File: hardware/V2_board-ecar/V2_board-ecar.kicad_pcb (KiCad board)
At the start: 2 copper layers, 160 x 100 mm, 90 parts, among them IC1 ATMEGA8A-P, J1 2x BATT IN, J10 24V, J11 18V, J12 5V, J13 Analog-in-2 0-5V, J14 IGBT, J15 Analog-in-3 - 30to5 (batt), J16 Mosfet Out (Fan), J17 2x Switch \n(to 5V), J18 Relay contacts, J19 2x 5V, J2 ST 2x GND, J3 2x 24V filtered, J4 ST 2x GND, J5 PWM-Signal, J6 LED ~3,2V 20mA, J7 Gas Pedal, J8 Gate, J9 BATT, K1 LEG-5, P1 ISP, Q1 BC547, Q2 IRFZ24N, Q3 BC547, U1 LM7818CT, U2 LM2576T-5, U3 TC429

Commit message: pcb: placed all parts
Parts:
- removed D8: D, Diode_THT:D_T-1_P12.70mm_Horizontal
- removed R2: nopop, Resistor_THT:R_Axial_DIN0922_L20.0mm_D9.0mm_P25.40mm_Horizontal
- added J20: ADC Battery, Connector_PinHeader_1.00mm:PinHeader_1x01_P1.00mm_Vertical, F.Cu at (101.0, 24.1)
- added J21: ADC reserve, Connector_PinHeader_1.00mm:PinHeader_1x01_P1.00mm_Vertical, F.Cu at (86.4, 24.1)
- added J22: ADC Gas-pedal, Connector_PinHeader_1.00mm:PinHeader_1x01_P1.00mm_Vertical, F.Cu at (71.8, 29.8)
- J17: value 2x Switch \n(to 5V) -> 2x Switch (to 5V)
- moved D12 154.3 mm to (42.7, 87.4), turned to 0 degrees
- moved C17 145.8 mm to (45.4, 82.9), turned to 0 degrees
- moved R27 140.1 mm to (67.8, 86.1), turned to 90 degrees
- moved R26 137.8 mm to (63.9, 86.1), turned to 90 degrees
- moved D13 128.4 mm to (78.4, 89.8), turned to 180 degrees
- moved R4 127.5 mm to (53.0, 53.8), turned to -90 degrees
- moved R24 127.5 mm to (52.8, 91.4), turned to 180 degrees
- moved C7 127.3 mm to (71.8, 75.3), turned to 0 degrees
- moved R22 126.9 mm to (52.8, 95.5), turned to 180 degrees
- moved C6 126.1 mm to (77.6, 52.7), turned to 180 degrees
- moved IC1 123.8 mm to (57.1, 64.1), turned to 90 degrees
- moved C18 123.1 mm to (76.0, 86.1), turned to 180 degrees
- moved R25 120.9 mm to (68.3, 93.2)
- moved R23 120.6 mm to (68.3, 96.4)
- moved C8 106.3 mm to (73.1, 80.1)
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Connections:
- J14 pad 1: Net-(J14-Pin_1) -> GND
- J14 pad 2: GND -> Net-(J14-Pin_2)
- J8 pad 1: Net-(J14-Pin_1) -> Net-(J14-Pin_2)
- U3 pad 6: Net-(J14-Pin_1) -> Net-(J14-Pin_2)
- U3 pad 7: Net-(J14-Pin_1) -> Net-(J14-Pin_2)
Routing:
- net Net-(J14-Pin_2): track 0.00 -> 13.9 mm
- net Net-(J14-Pin_1): track 13.9 -> 0.00 mm
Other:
- board text added: "${REFERENCE}"

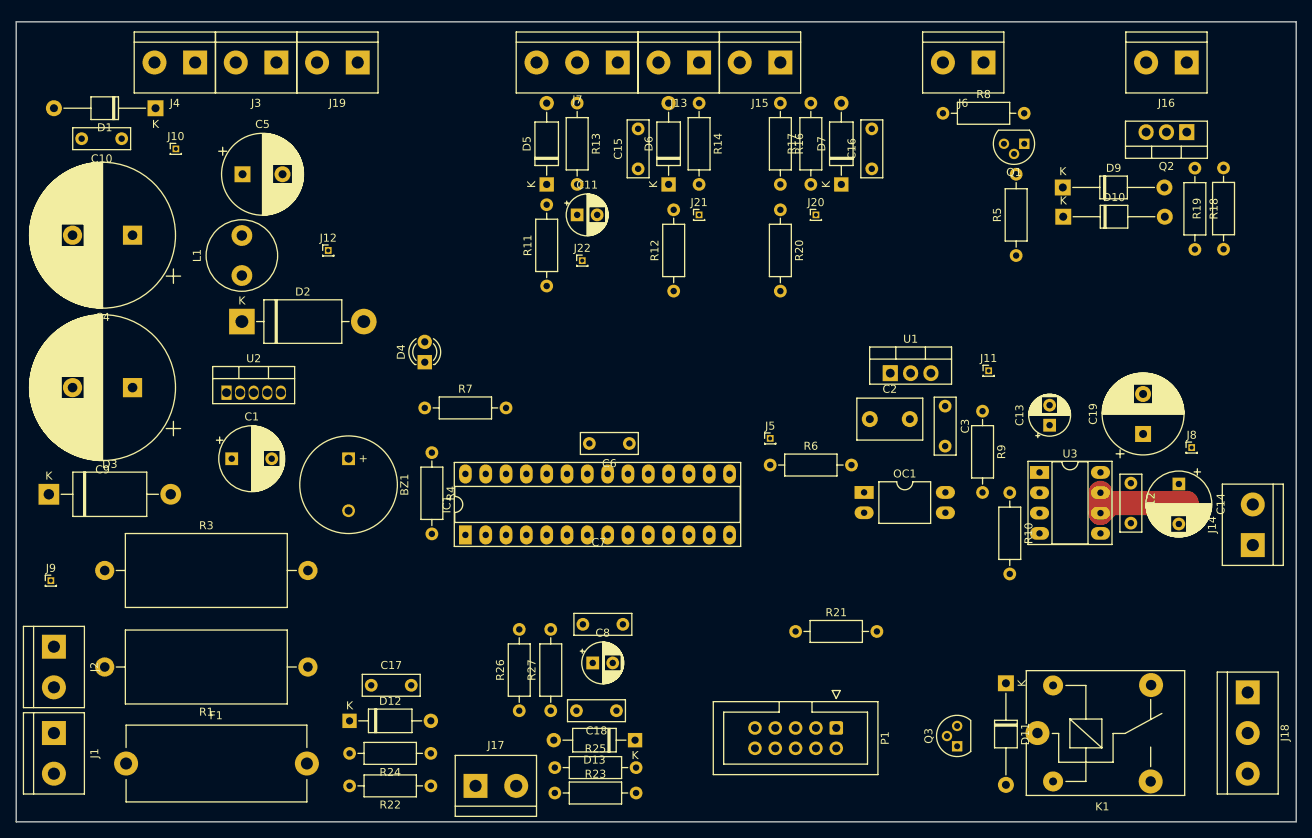
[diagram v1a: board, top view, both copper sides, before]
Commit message: pcb: Add moutingholes, fuses
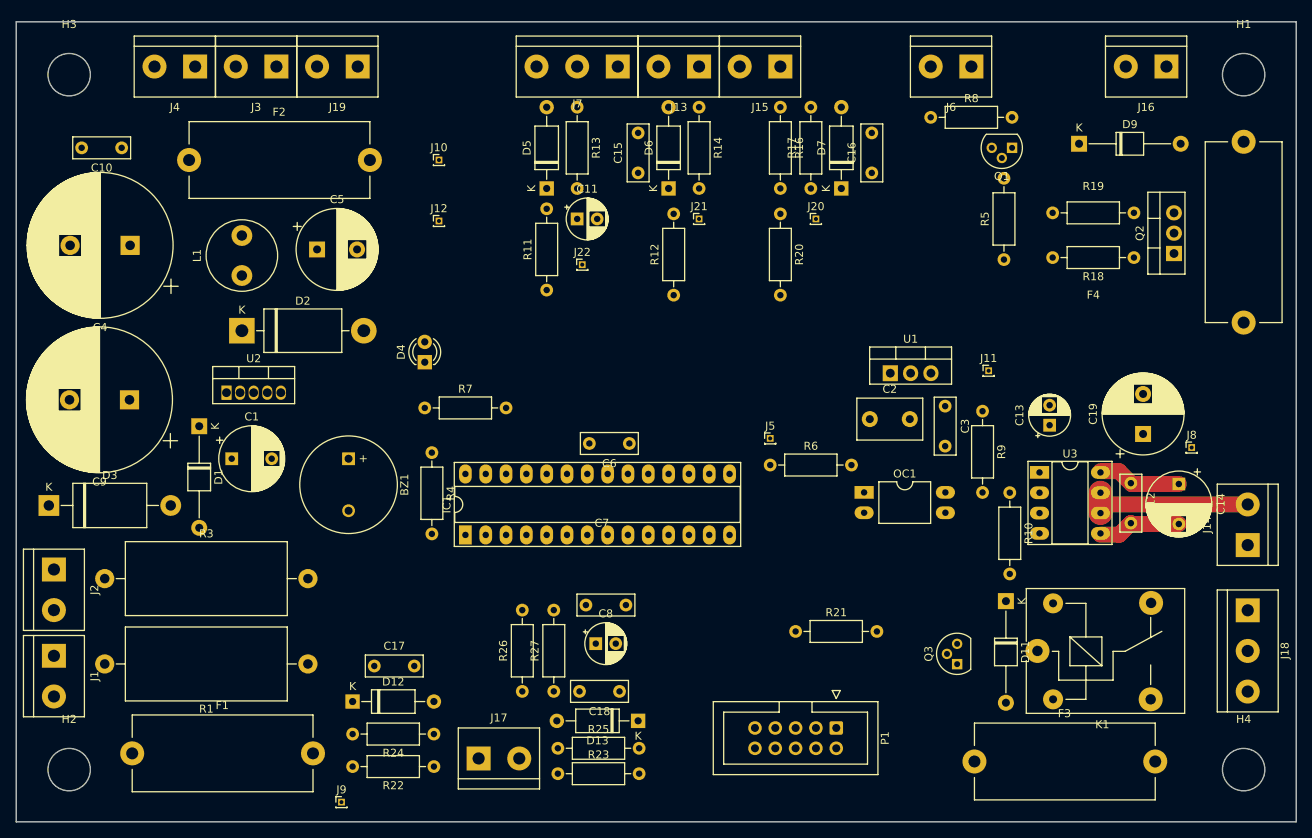
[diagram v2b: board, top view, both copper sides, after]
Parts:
- removed D10: D, Diode_THT:D_T-1_P12.70mm_Horizontal
- added F2: 500mA, Fuse:Fuseholder_Cylinder-5x20mm_Stelvio-Kontek_PTF78_Horizontal_Open, F.Cu at (22.6, 17.3)
- added F3: 500mA, Fuse:Fuseholder_Cylinder-5x20mm_Stelvio-Kontek_PTF78_Horizontal_Open, F.Cu at (120.8, 92.5)
- added F4: 500mA, Fuse:Fuseholder_Cylinder-5x20mm_Stelvio-Kontek_PTF78_Horizontal_Open, F.Cu at (154.4, 37.6)
- added H1: MountingHole, MountingHole:MountingHole_5.3mm_M5, F.Cu at (154.4, 6.60)
- added H2: MountingHole, MountingHole:MountingHole_5.3mm_M5, F.Cu at (7.62, 93.5)
- added H3: MountingHole, MountingHole:MountingHole_5.3mm_M5, F.Cu at (7.62, 6.60)
- added H4: MountingHole, MountingHole:MountingHole_5.3mm_M5, F.Cu at (154.4, 93.5)
- J16: value Mosfet Out (Fan) -> Mosfet Out (Diode, Mosfet)
- moved J9 45.7 mm to (41.7, 97.5)
- moved D1 40.1 mm to (23.9, 50.5), turned to -90 degrees
- moved J10 32.9 mm to (53.8, 17.3)
- moved R19 21.8 mm to (130.6, 23.9), turned to 0 degrees
- moved Q2 15.3 mm to (145.7, 29.0), turned to 90 degrees
- moved J12 14.3 mm to (53.8, 24.9)
- moved R18 13.5 mm to (140.7, 29.5), turned to 180 degrees
- moved C5 13.2 mm to (38.6, 28.4)
- moved D11 10.3 mm to (124.7, 72.4)
- moved K1 10.3 mm to (128.7, 78.6)
- moved J18 10.3 mm to (154.9, 73.6)
- moved Q3 10.3 mm to (118.6, 80.3)
- moved J1 9.65 mm to (5.71, 79.2)
- moved J2 9.65 mm to (5.71, 68.5)
- moved D9 5.83 mm to (133.9, 15.2)
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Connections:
- C10 pad 1: +24V filtered -> Net-(D1-K)
- C4 pad 1: +24V filtered -> Net-(D1-K)
- C9 pad 1: +24V filtered -> Net-(D1-K)
- D1 pad 1: +24V filtered -> Net-(D1-K)
- D3 pad 2: +24V filtered -> Net-(D1-K)
- D9 pad 1: +24V filtered -> Net-(D9-K)
- D9 pad 2: Net-(D10-A) -> Net-(D9-A)
- J16 pad 1: Net-(D10-A) -> Net-(D9-A)
- J16 pad 2: +24V filtered -> Net-(D9-K)
- K1 pad 1: Net-(J18-Pin_2) -> Net-(F3-Pad1)
- Q2 pad 2: Net-(D10-A) -> Net-(Q2-D)
- R3 pad 2: +24V filtered -> Net-(D1-K)
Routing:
- net +18V: track 0.00 -> 10.5 mm
- net GND: track 0.00 -> 10.4 mm
- net Net-(J14-Pin_2): track 13.9 -> 21.4 mm

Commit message: pcb: layout complete (for review)
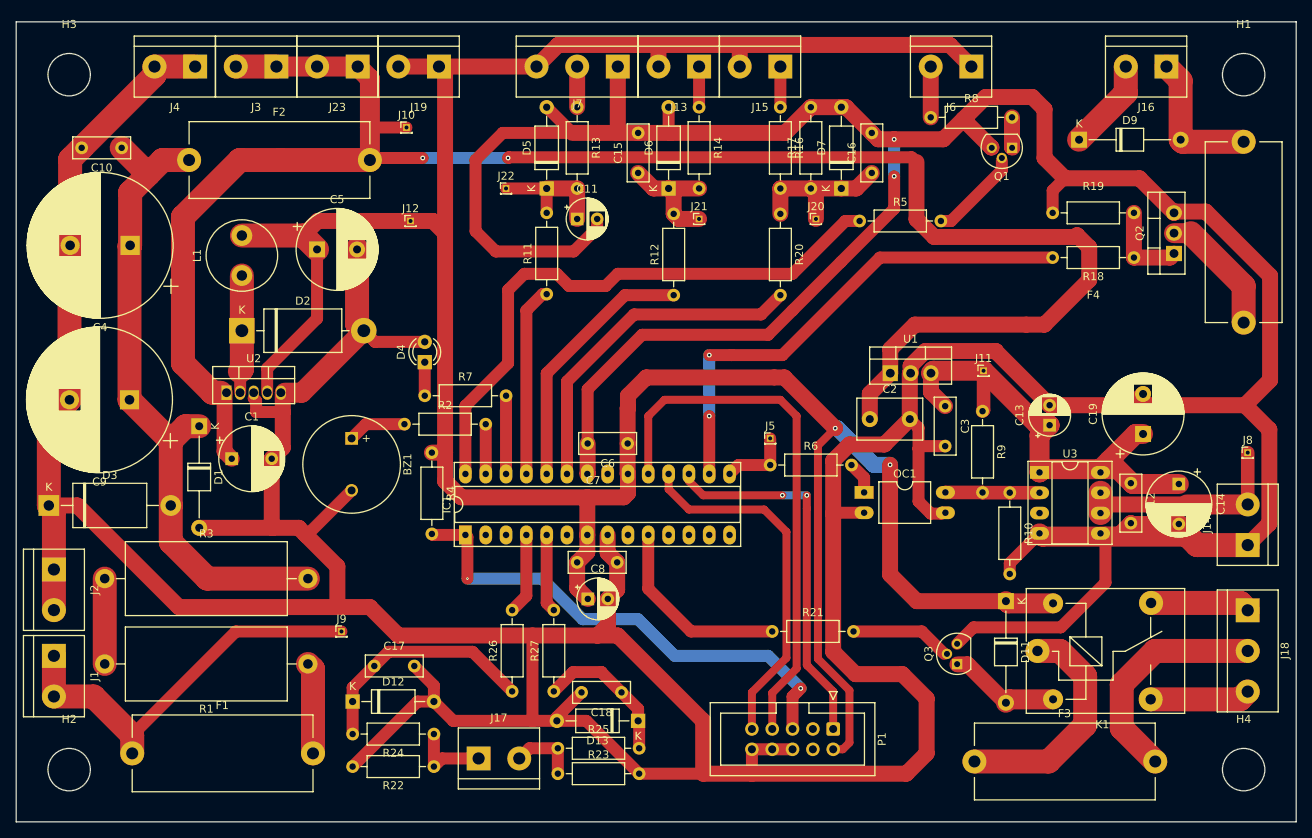
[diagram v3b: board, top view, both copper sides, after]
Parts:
- added J23: 2x 24V filtered, TerminalBlock:TerminalBlock_bornier-2_P5.08mm, F.Cu at (43.7, 5.59)
- added R2: 10, Resistor_THT:R_Axial_DIN0207_L6.3mm_D2.5mm_P10.16mm_Horizontal, F.Cu at (49.5, 50.3)
- moved J9 21.3 mm to (41.7, 76.2)
- moved R5 18.7 mm to (106.4, 24.9), turned to 0 degrees
- moved J22 13.5 mm to (62.2, 20.8)
- moved J19 10.2 mm to (53.8, 5.59)
- moved J8 7.04 mm to (154.9, 53.8)
- moved J10 5.75 mm to (49.8, 13.2)
- moved C8 5.68 mm to (72.5, 72.1)
- moved C7 5.45 mm to (71.1, 67.6)
- moved J12 3.56 mm to (50.3, 24.9)
- moved R21 2.92 mm to (95.5, 76.2)
- moved BZ1 2.57 mm to (42.9, 52.1)
- moved R7 1.52 mm to (52.1, 46.7)
- moved R26 1.27 mm to (63.0, 83.7)
- moved J11 0.64 mm to (121.9, 43.6)
- moved R11 0.51 mm to (67.3, 34.0)
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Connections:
- BZ1 pad 1: /BUZZER -> Net-(BZ1-+)
- IC1 pad 16: unconnected-(IC1-(~{SS}/OC1B)PB2-Pad16) -> /Mosfet (fan)
- IC1 pad 23: /analog0 (gas) -> /analog2 (30V Batt)
- IC1 pad 25: /analog2 (30V Batt) -> /analog0 (gas)
- IC1 pad 9: /Mosfet (fan) -> unconnected-(IC1-PB6(XTAL1/TOSC1)-Pad9)
- J15 pad 2: +24V filtered -> +5V
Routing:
- net GND: track 10.4 -> 880.1 mm, vias 0 -> 2
- net +5V: track 0.00 -> 352.2 mm, vias 0 -> 2
- net +24V filtered: track 0.00 -> 233.0 mm, vias 0 -> 2
- net Net-(D1-K): track 0.00 -> 83.0 mm
- net /LED-ext: track 0.00 -> 74.0 mm
- net /SCK: track 0.00 -> 67.8 mm
- net /Mosfet (fan): track 0.00 -> 62.8 mm, vias 0 -> 2
- net /RESET: track 0.00 -> 62.6 mm, vias 0 -> 2
- net +18V: track 10.5 -> 69.5 mm
- net +BATT: track 0.00 -> 50.7 mm
- net /MOSI: track 0.00 -> 46.9 mm, vias 0 -> 2
- net /MISO: track 0.00 -> 45.3 mm
- net /analog2 (30V Batt): track 0.00 -> 42.7 mm
- net /analog1: track 0.00 -> 32.5 mm
- net Net-(D12-K): track 0.00 -> 29.7 mm
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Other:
- board text removed: "${REFERENCE}"

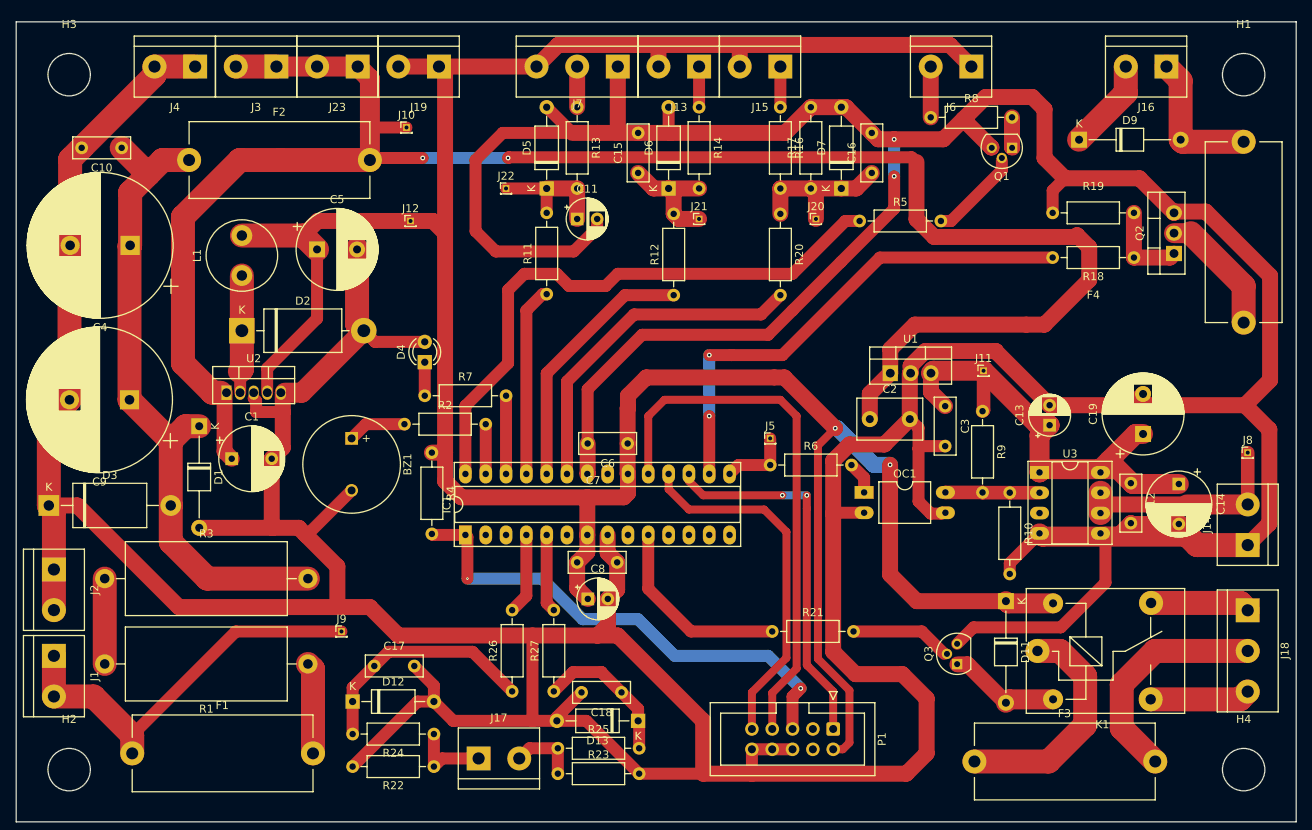
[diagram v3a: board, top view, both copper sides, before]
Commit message: pcb: minor optimizations, swap layers
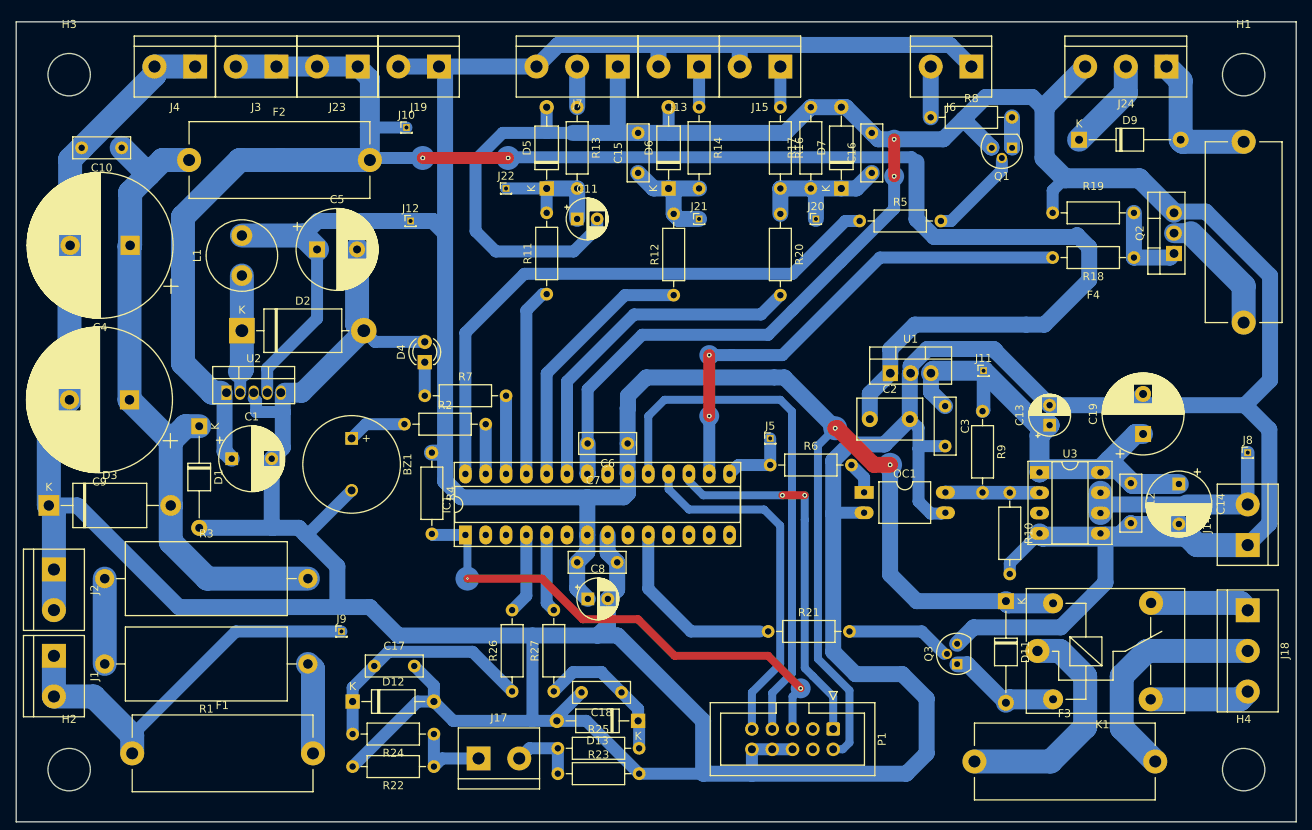
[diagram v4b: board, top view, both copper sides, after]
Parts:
- removed J16: Mosfet Out (Diode, Mosfet), TerminalBlock:TerminalBlock_bornier-2_P5.08mm
- added J24: GND-supp, Diode, Mosfet (fan), TerminalBlock:TerminalBlock_bornier-3_P5.08mm, F.Cu at (144.8, 5.59)
- moved R21 0.51 mm to (95.0, 76.2)
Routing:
- net GND: track 880.1 -> 886.4 mm
- net /Relay (light): track 24.4 -> 22.9 mm
- net /LED-ext: track 74.0 -> 72.7 mm
- net /MISO: track 45.3 -> 44.6 mm
- net Net-(J18-Pin_2): track 28.9 -> 29.5 mm
- net Net-(Q3-B): track 12.5 -> 13.0 mm

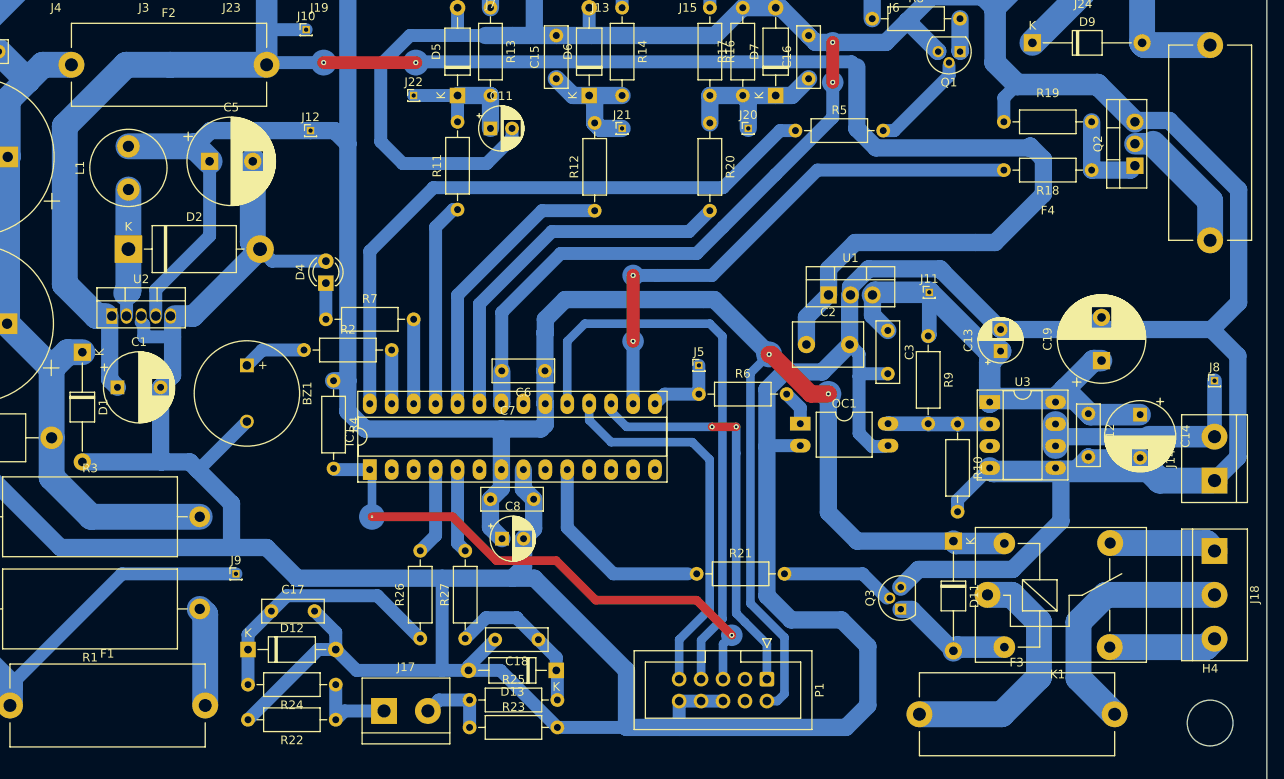
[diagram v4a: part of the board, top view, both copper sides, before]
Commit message: pcb: re-arrange schematic, fix track widths
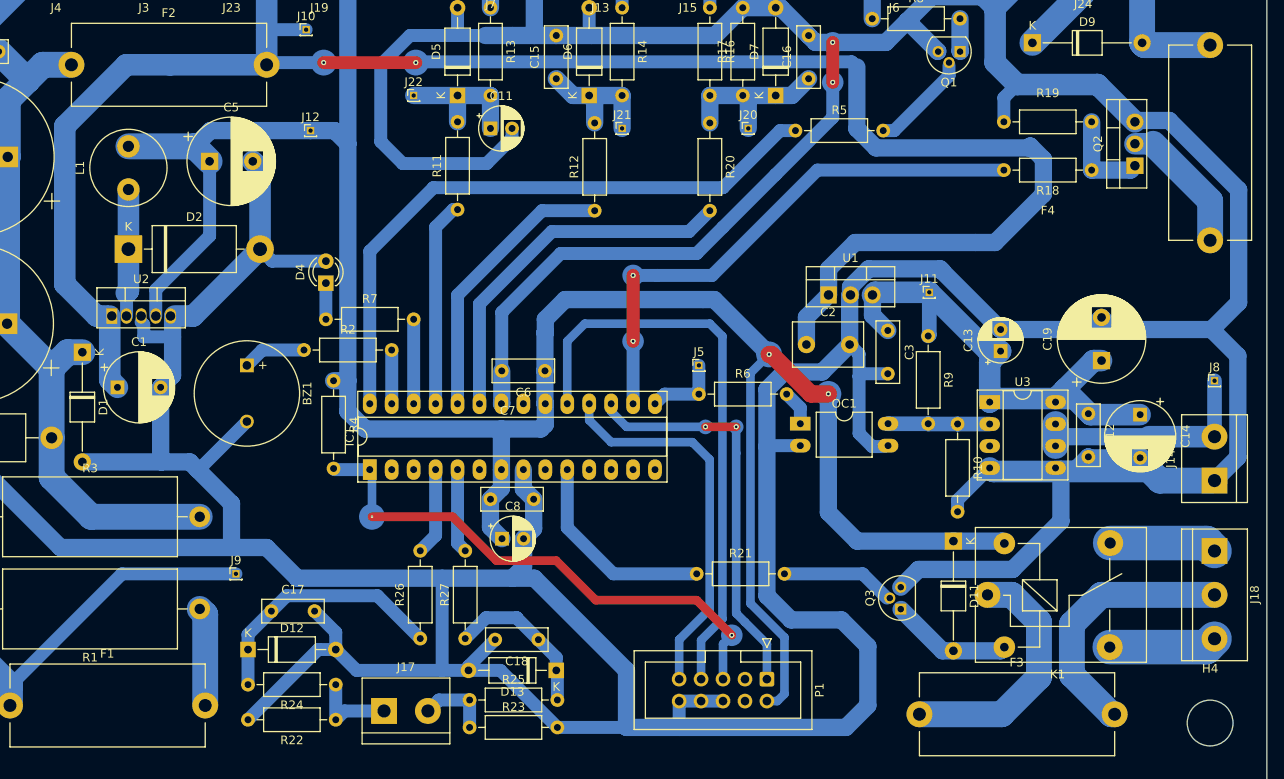
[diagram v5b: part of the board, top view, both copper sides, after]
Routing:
- net GND: track 886.4 -> 888.5 mm
- net Net-(J18-Pin_2): track 29.5 -> 30.6 mm
- net /Relay (light): track 22.9 -> 23.9 mm
- net Net-(D7-K): track 19.5 -> 18.6 mm
